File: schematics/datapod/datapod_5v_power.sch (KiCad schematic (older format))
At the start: 10 parts, among them J5 Conn_02x02_Odd_Even, U5 LT1374CS8-5PBF

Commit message: modified schematic
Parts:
- U5: symbol LT1374CS8-5PBF:LT1374CS8-5PBF -> datapod-rescue:LT1374CS8-5PBF-LT1374CS8-5PBF
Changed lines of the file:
@@
 $EndDescr
 $Comp
-L LT1374CS8-5PBF:LT1374CS8-5PBF U5
+L datapod-rescue:LT1374CS8-5PBF-LT1374CS8-5PBF U5
 U 1 1 5E424E08
 P 4400 3050
+AR Path="/5E424E08" Ref="U5"  Part="1"
+AR Path="/5E423883/5E424E08" Ref="U5"  Part="1"
 F 0 "U5" H 6000 3415 50  0000 C CNN
 F 1 "LT1374CS8-5PBF" H 6000 3324 50  0000 C CNN

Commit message: added more connectors and started drawing the PCB
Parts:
- removed U5: LT1374CS8-5PBF, Package_SO:SO-8_3.9x4.9mm_P1.27mm, symbol datapod-rescue:LT1374CS8-5PBF-LT1374CS8-5PBF
- added U5: LT1374CS8-5PBF, Package_SO:SO-8_3.9x4.9mm_P1.27mm, symbol LT1374CS8-5PBF:LT1374CS8-5PBF
- J7: renamed from J5; footprint Connector_Molex:Molex_Mini-Fit_Jr_5566-04A2_2x02_P4.20mm_Vertical -> Connector_Molex:Molex_Mini-Fit_Sr_42819-22XX_1x02_P10.00mm_Vertical; symbol Connector_Generic:Conn_02x02_Odd_Even -> Connector_Generic:Conn_01x02; Part# 23-0039299043-ND -> WM11908-ND
- renumbered D7 to D5, D8 to D6
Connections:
- wire segments 45 -> 41
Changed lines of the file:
@@
 $EndDescr
 $Comp
-L datapod-rescue:LT1374CS8-5PBF-LT1374CS8-5PBF U5
-U 1 1 5E424E08
-P 4400 3050
-AR Path="/5E424E08" Ref="U5"  Part="1"
-AR Path="/5E423883/5E424E08" Ref="U5"  Part="1"
-F 0 "U5" H 6000 3415 50  0000 C CNN
-F 1 "LT1374CS8-5PBF" H 6000 3324 50  0000 C CNN
-F 2 "Package_SO:SO-8_3.9x4.9mm_P1.27mm" H 4725 4450 50  0001 L BNN
-F 3 "Linear Technology" H 4700 3875 50  0001 L BNN
-F 4 "SO-8 Linear Technology" H 4650 4050 50  0001 L BNN "Field4"
-F 5 "https://www.digikey.com/product-detail/en/linear-technology-analog-devices/LT1374CS8-5-PBF/LT1374CS8-5-PBF-ND/888771?utm_source=snapeda&utm_medium=aggregator&utm_campaign=symbol" H 4675 3600 50  0001 L BNN "Field5"
-F 6 "LT1374 - 4.5A, 500kHz Step-Down Switching Regulator" H 4675 3725 50  0001 L BNN "Field6"
-F 7 "LT1374CS8-5#PBF" H 4700 4175 50  0001 L BNN "Field7"
-F 8 "LT1374CS8-5#PBF-ND" H 4725 4300 50  0001 L BNN "Part#"
-	1    4400 3050
-	1    0    0    -1
-$EndComp
-$Comp
-L power:VCC #PWR0137
+L power:VCC #PWR042
 U 1 1 5E425B31
 P 3950 2200
-F 0 "#PWR0137" H 3950 2050 50  0001 C CNN
+F 0 "#PWR042" H 3950 2050 50  0001 C CNN
 F 1 "VCC" H 3967 2373 50  0000 C CNN
 F 2 "" H 3950 2200 50  0001 C CNN
@@
 	4400 3250 2150 3250
 $Comp
-L power:GND #PWR0138
+L power:GND #PWR045
 U 1 1 5E42FAE4
 P 2150 3900
-F 0 "#PWR0138" H 2150 3650 50  0001 C CNN
+F 0 "#PWR045" H 2150 3650 50  0001 C CNN
 F 1 "GND" H 2155 3727 50  0000 C CNN
 F 2 "" H 2150 3900 50  0001 C CNN
@@
 P 10300 2300
 AR Path="/5E43B693" Ref="#PWR?"  Part="1"
-AR Path="/5E423883/5E43B693" Ref="#PWR0139"  Part="1"
-F 0 "#PWR0139" H 10300 2150 50  0001 C CNN
+AR Path="/5E423883/5E43B693" Ref="#PWR043"  Part="1"
+F 0 "#PWR043" H 10300 2150 50  0001 C CNN
 F 1 "+5V" H 10315 2473 50  0000 C CNN
 F 2 "" H 10300 2300 50  0001 C CNN
@@
 NoConn ~ 7600 3150
 $Comp
-L Device:D_Schottky D8
+L Device:D_Schottky D6
 U 1 1 5E43F6C8
 P 9400 3450
-F 0 "D8" V 9450 3600 50  0000 C CNN
+F 0 "D6" V 9450 3600 50  0000 C CNN
 F 1 "MBRS340" V 9550 3750 50  0000 C CNN
 F 2 "Diode_SMD:D_SMC" H 9400 3450 50  0001 C CNN
@@
 $EndComp
 $Comp
-L Device:D_Schottky D7
+L Device:D_Schottky D5
 U 1 1 5E43FA0D
 P 9900 2600
-F 0 "D7" H 9900 2816 50  0000 C CNN
+F 0 "D5" H 9900 2816 50  0000 C CNN
 F 1 "1N914BWT" H 9900 2725 50  0000 C CNN
 F 2 "Diode_SMD:D_SOD-523" H 9900 2600 50  0001 C CNN
@@
 $EndComp
 $Comp
-L power:GND #PWR0140
+L power:GND #PWR044
 U 1 1 5E446F4A
 P 9400 3850
-F 0 "#PWR0140" H 9400 3600 50  0001 C CNN
+F 0 "#PWR044" H 9400 3600 50  0001 C CNN
 F 1 "GND" H 9405 3677 50  0000 C CNN
 F 2 "" H 9400 3850 50  0001 C CNN
@@
 P 1500 6500
 AR Path="/5E45849C" Ref="#PWR?"  Part="1"
-AR Path="/5E423883/5E45849C" Ref="#PWR0141"  Part="1"
-F 0 "#PWR0141" H 1500 6350 50  0001 C CNN
+AR Path="/5E423883/5E45849C" Ref="#PWR046"  Part="1"
+F 0 "#PWR046" H 1500 6350 50  0001 C CNN
 F 1 "+5V" H 1515 6673 50  0000 C CNN
 F 2 "" H 1500 6500 50  0001 C CNN
@@
 P 1500 7000
 AR Path="/5E4584A2" Ref="#PWR?"  Part="1"
-AR Path="/5E423883/5E4584A2" Ref="#PWR0142"  Part="1"
-F 0 "#PWR0142" H 1500 6750 50  0001 C CNN
+AR Path="/5E423883/5E4584A2" Ref="#PWR047"  Part="1"
+F 0 "#PWR047" H 1500 6750 50  0001 C CNN
 F 1 "GND" H 1505 6827 50  0000 C CNN
 F 2 "" H 1500 7000 50  0001 C CNN
@@
 	1500 6900 1700 6900
 $Comp
-L Connector_Generic:Conn_02x02_Odd_Even J?
+L Connector_Generic:Conn_01x02 J?
 U 1 1 5E790D06
 P 1300 1050
 AR Path="/5E14D46E/5E790D06" Ref="J?"  Part="1"
-AR Path="/5E423883/5E790D06" Ref="J5"  Part="1"
-F 0 "J5" H 1350 1267 50  0000 C CNN
+AR Path="/5E423883/5E790D06" Ref="J7"  Part="1"
+F 0 "J7" H 1350 1267 50  0000 C CNN
 F 1 "Conn_02x02_Odd_Even" H 1350 1176 50  0000 C CNN
-F 2 "Connector_Molex:Molex_Mini-Fit_Jr_5566-04A2_2x02_P4.20mm_Vertical" H 1300 1050 50  0001 C CNN
-F 3 "~" H 1300 1050 50  0001 C CNN
+F 2 "Connector_Molex:Molex_Mini-Fit_Sr_42819-22XX_1x02_P10.00mm_Vertical" H 1300 1050 50  0001 C CNN
+F 3 "https://www.molex.com/pdm_docs/ps/PS-42815-001.pdf" H 1300 1050 50  0001 C CNN
 F 4 "Digikey" H 1300 1050 50  0001 C CNN "Vendor"
-F 5 "23-0039299043-ND" H 1300 1050 50  0001 C CNN "Part#"
+F 5 "WM11908-ND" H 1300 1050 50  0001 C CNN "Part#"
 	1    1300 1050
 	1    0    0    -1
 $EndComp
 $Comp
-L power:VCC #PWR0113
+L power:VCC #PWR040
 U 1 1 5E791421
 P 650 900
-F 0 "#PWR0113" H 650 750 50  0001 C CNN
+F 0 "#PWR040" H 650 750 50  0001 C CNN
 F 1 "VCC" H 667 1073 50  0000 C CNN
 F 2 "" H 650 900 50  0001 C CNN
@@
 Wire Wire Line
 	650  1050 650  900
-Wire Wire Line
-	1100 1150 650  1150
-Wire Wire Line
-	650  1150 650  1050
-Connection ~ 650  1050
-$Comp
-L power:GND #PWR0117
+$Comp
+L power:GND #PWR041
 U 1 1 5E792A30
-P 2100 1200
-F 0 "#PWR0117" H 2100 950 50  0001 C CNN
-F 1 "GND" H 2105 1027 50  0000 C CNN
-F 2 "" H 2100 1200 50  0001 C CNN
-F 3 "" H 2100 1200 50  0001 C CNN
-	1    2100 1200
-	1    0    0    -1
-$EndComp
-Wire Wire Line
-	1600 1050 2100 1050
-Wire Wire Line
-	2100 1050 2100 1150
-Wire Wire Line
-	1600 1150 2100 1150
-Connection ~ 2100 1150
-Wire Wire Line
-	2100 1150 2100 1200
+P 650 1300
+F 0 "#PWR041" H 650 1050 50  0001 C CNN
+F 1 "GND" H 655 1127 50  0000 C CNN
+F 2 "" H 650 1300 50  0001 C CNN
+F 3 "" H 650 1300 50  0001 C CNN
+	1    650  1300
+	1    0    0    -1
+$EndComp
 Text Notes 850  1400 0    50   ~ 0
 BATTERY PACK CONNECTS\nTO THIS BOARD CONNECTOR
+$Comp
+L LT1374CS8-5PBF:LT1374CS8-5PBF U5
+U 1 1 5DC5BD7C
+P 4400 3050
+F 0 "U5" H 6000 3415 50  0000 C CNN
+F 1 "LT1374CS8-5PBF" H 6000 3324 50  0000 C CNN
+F 2 "Package_SO:SO-8_3.9x4.9mm_P1.27mm" H 4725 4450 50  0001 L BNN
+F 3 "Linear Technology" H 4700 3875 50  0001 L BNN
+F 4 "SO-8 Linear Technology" H 4650 4050 50  0001 L BNN "Field4"
+F 5 "https://www.digikey.com/product-detail/en/linear-technology-analog-devices/LT1374CS8-5-PBF/LT1374CS8-5-PBF-ND/888771?utm_source=snapeda&utm_medium=aggregator&utm_campaign=symbol" H 4675 3600 50  0001 L BNN "Field5"
+F 6 "LT1374 - 4.5A, 500kHz Step-Down Switching Regulator" H 4675 3725 50  0001 L BNN "Field6"
+F 7 "LT1374CS8-5#PBF" H 4700 4175 50  0001 L BNN "Field7"
+F 8 "LT1374CS8-5#PBF-ND" H 4725 4300 50  0001 L BNN "Part#"
+	1    4400 3050
+	1    0    0    -1
+$EndComp
+Wire Wire Line
+	1100 1150 650  1150
+Wire Wire Line
+	650  1150 650  1300
 $EndSCHEMATC

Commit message: added final routed PCB, gerbers and BOM
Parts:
- C17, C18: Part# (none) -> TCJA106M025R0150; part# TCJA106M025R0150 -> (none)
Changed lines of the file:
@@
 F 3 "http://datasheets.avx.com/TCJ.pdf" H 1300 6750 50  0001 C CNN
 F 4 "Digikey" H 1300 6750 50  0001 C CNN "Vendor"
-F 5 "TCJA106M025R0150" H 1300 6750 50  0001 C CNN "part#"
+F 5 "TCJA106M025R0150" H 1300 6750 50  0001 C CNN "Part#"
 	1    1300 6750
 	1    0    0    -1
@@
 F 3 "http://datasheets.avx.com/TCJ.pdf" H 1700 6750 50  0001 C CNN
 F 4 "Digikey" H 1700 6750 50  0001 C CNN "Vendor"
-F 5 "TCJA106M025R0150" H 1700 6750 50  0001 C CNN "part#"
+F 5 "TCJA106M025R0150" H 1700 6750 50  0001 C CNN "Part#"
 	1    1700 6750
 	1    0    0    -1

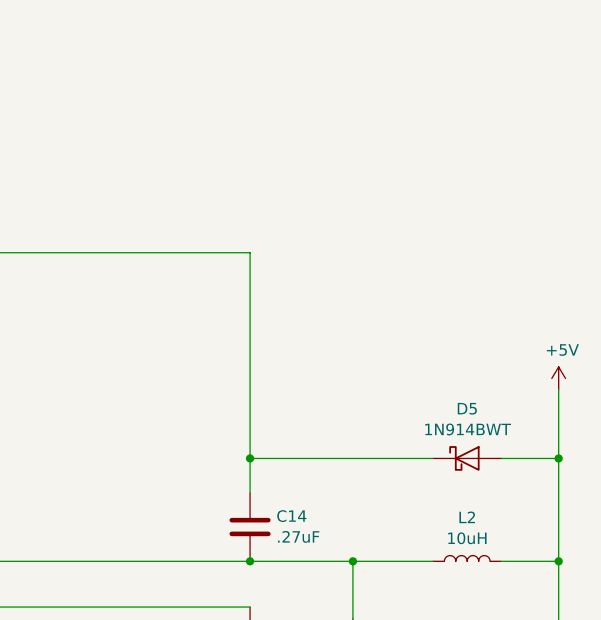
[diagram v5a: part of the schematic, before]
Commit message: fixed bad gnd trace on 3.3v circuit and added comments to the silkscreen
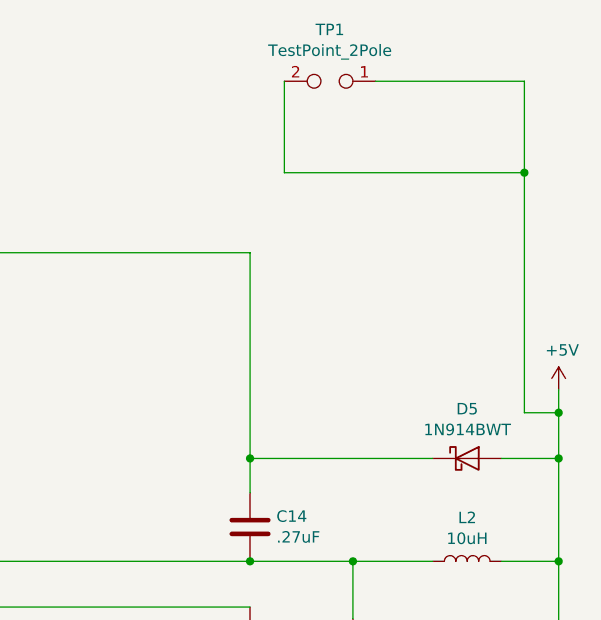
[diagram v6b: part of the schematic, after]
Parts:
- added TP1: TestPoint_2Pole, TestPoint:TestPoint_2Pads_Pitch5.08mm_Drill1.3mm, symbol Connector:TestPoint_2Pole
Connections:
- net +5V: now also TP1.1, TP1.2
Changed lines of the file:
@@
 Connection ~ 10300 2600
 Wire Wire Line
-	10300 2600 10300 2300
+	10300 2600 10300 2400
 Wire Wire Line
 	9750 2600 8950 2600
@@
 Wire Wire Line
 	650  1150 650  1300
+$Comp
+L Connector:TestPoint_2Pole TP1
+U 1 1 5E26F000
+P 9300 950
+F 0 "TP1" H 9300 725 50  0000 C CNN
+F 1 "TestPoint_2Pole" H 9300 816 50  0000 C CNN
+F 2 "TestPoint:TestPoint_2Pads_Pitch5.08mm_Drill1.3mm" H 9300 950 50  0001 C CNN
+F 3 "~" H 9300 950 50  0001 C CNN
+	1    9300 950
+	-1   0    0    1
+$EndComp
+Wire Wire Line
+	9500 950  10150 950
+Wire Wire Line
+	10150 950  10150 1350
+Wire Wire Line
+	10150 2400 10300 2400
+Connection ~ 10300 2400
+Wire Wire Line
+	10300 2400 10300 2300
+Wire Wire Line
+	9100 950  9100 1350
+Wire Wire Line
+	9100 1350 10150 1350
+Connection ~ 10150 1350
+Wire Wire Line
+	10150 1350 10150 2400
 $EndSCHEMATC
